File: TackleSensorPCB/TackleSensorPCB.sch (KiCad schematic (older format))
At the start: 26 parts, among them J1 PJ-037A, J2 Conn_01x03_Male, J3 Conn_01x04_Male, J4 Conn_01x07_Male, Q1 2N7002, Q2 2N7002, SW1 SW_DPST_x2, U1 TPS62172DSG, U2 MSP430FR2433IRGER, U3 MMA8452QR1

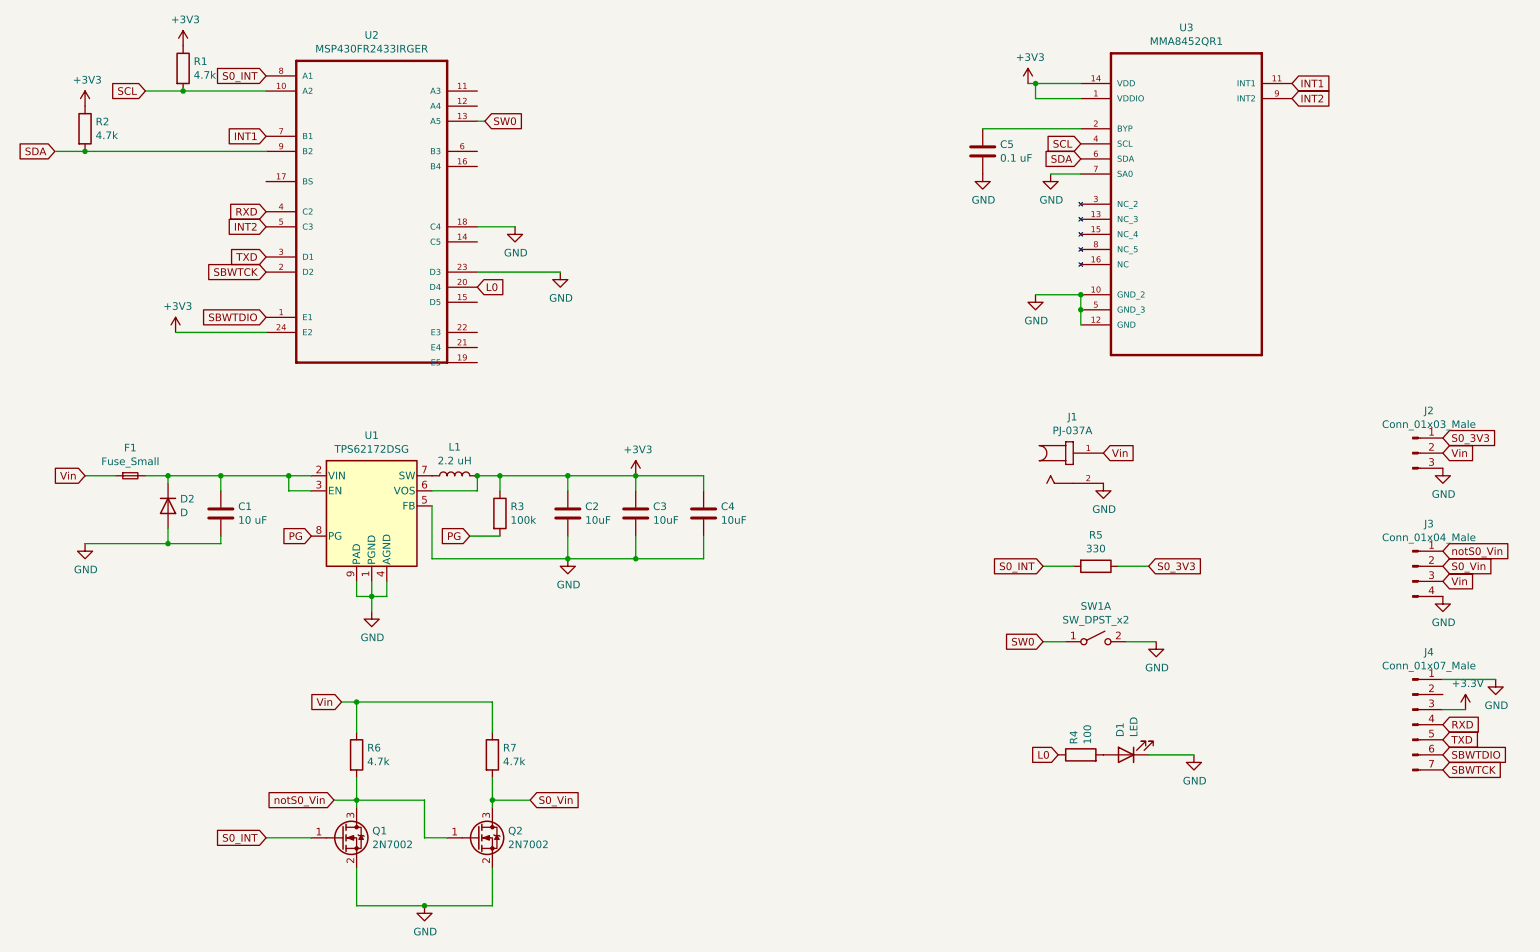
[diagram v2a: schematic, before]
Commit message: Updated to LS2
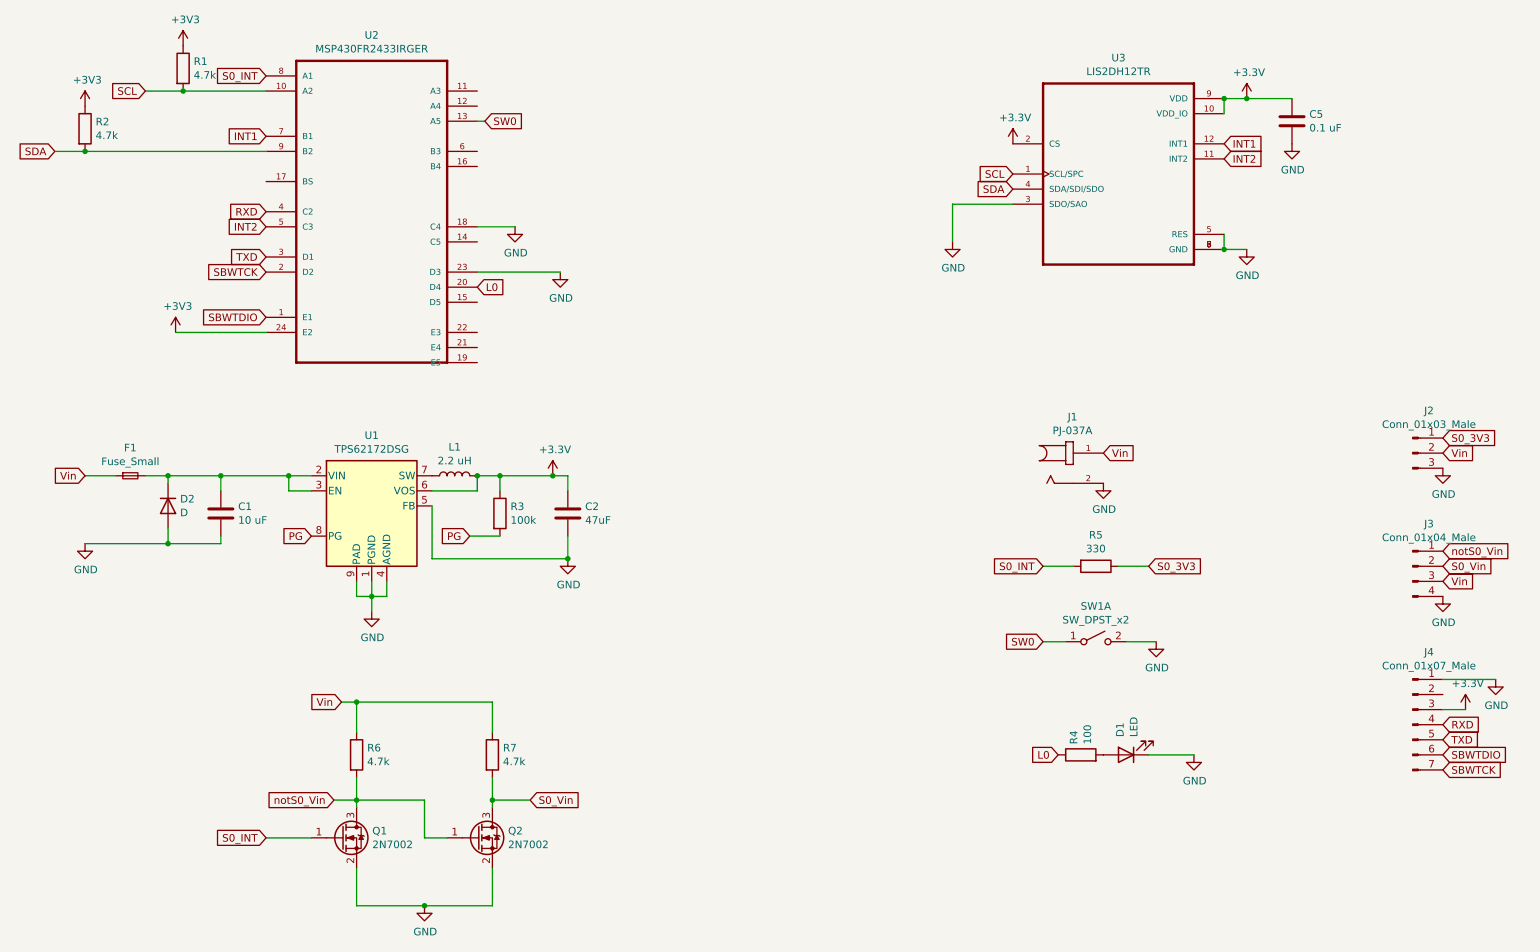
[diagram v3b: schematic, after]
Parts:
- removed C3, C4: 10uF, Capacitor_SMD:C_0402_1005Metric, symbol Device:C
- removed U3: MMA8452QR1, MMA8452QR1:QFN50P300X300X100-16N, symbol MMA8452QR1:MMA8452QR1
- added U3: LIS2DH12TR, LIS2DH12TR:PQFN50P200X200100-12N, symbol LIS2DH12TR:LIS2DH12TR
- C2: value 10uF -> 47uF
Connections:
- net +3V3: now also C5.1, U3.10 (VDD_IO), U3.2 (CS), U3.9 (VDD)
- net GND: now also U3.3 (SDO/SAO), U3.5 (RES), U3.6 (GND), U3.7 (GND), U3.8 (GND)
- net INT1: now also U3.12 (INT1)
- net INT2: now also U3.11 (INT2)
- net SCL: now also U3.1 (SCL/SPC)
- net SDA: now also U3.4 (SDA/SDI/SDO)
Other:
- moved on the sheet: C5
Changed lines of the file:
@@
-$EndComp
-$Comp
-L MMA8452QR1:MMA8452QR1 U3
-U 1 1 5F828B59
-P 8300 2300
-F 0 "U3" H 8300 3370 50  0000 C CNN
-F 1 "MMA8452QR1" H 8300 3279 50  0000 C CNN
-F 2 "MMA8452QR1:QFN50P300X300X100-16N" H 8300 2300 50  0001 L BNN
-F 3 "Freescale" H 8300 2300 50  0001 L BNN
-F 4 "QFN-16" H 8300 2300 50  0001 L BNN "Field4"
-F 5 "MMA8452QR1" H 8300 2300 50  0001 L BNN "Field5"
-F 6 "1908022" H 8300 2300 50  0001 L BNN "Field6"
-F 7 "84R7352" H 8300 2300 50  0001 L BNN "Field7"
-	1    8300 2300
-	1    0    0    -1
 $EndComp
 $Comp
@@
 Wire Wire Line
 	3300 4750 3300 4400
-$Comp
-L power:+3V3 #PWR08
-U 1 1 5F839D50
-P 4650 4200
-F 0 "#PWR08" H 4650 4050 50  0001 C CNN
-F 1 "+3V3" H 4665 4373 50  0000 C CNN
-F 2 "" H 4650 4200 50  0001 C CNN
-F 3 "" H 4650 4200 50  0001 C CNN
-	1    4650 4200
-	1    0    0    -1
-$EndComp
-Text GLabel 9000 1600 2    50   Input ~ 0
+Text GLabel 8550 2000 2    50   Input ~ 0
 INT1
-Text GLabel 9000 1700 2    50   Input ~ 0
+Text GLabel 8550 2100 2    50   Input ~ 0
 INT2
 Wire Wire Line
@@
 	1    0    0    -1
 $EndComp
-Wire Wire Line
-	7250 1600 7300 1600
-$Comp
-L power:+3V3 #PWR010
-U 1 1 5F83E38F
-P 7250 1600
-F 0 "#PWR010" H 7250 1450 50  0001 C CNN
-F 1 "+3V3" H 7265 1773 50  0000 C CNN
-F 2 "" H 7250 1600 50  0001 C CNN
-F 3 "" H 7250 1600 50  0001 C CNN
-	1    7250 1600
-	1    0    0    -1
-$EndComp
-Wire Wire Line
-	7600 1700 7300 1700
-Wire Wire Line
-	7300 1700 7300 1600
-Connection ~ 7300 1600
-Wire Wire Line
-	7300 1600 7600 1600
-Wire Wire Line
-	7600 2200 7400 2200
-$Comp
-L power:GND #PWR012
-U 1 1 5F8405C5
-P 7400 2200
-F 0 "#PWR012" H 7400 1950 50  0001 C CNN
-F 1 "GND" H 7405 2027 50  0000 C CNN
-F 2 "" H 7400 2200 50  0001 C CNN
-F 3 "" H 7400 2200 50  0001 C CNN
-	1    7400 2200
-	1    0    0    -1
-$EndComp
 $Comp
 L Device:C C5
 U 1 1 5F841354
-P 6950 2050
-F 0 "C5" H 7065 2096 50  0000 L CNN
-F 1 "0.1 uF" H 7065 2005 50  0000 L CNN
-F 2 "Capacitor_SMD:C_0402_1005Metric" H 6988 1900 50  0001 C CNN
-F 3 "~" H 6950 2050 50  0001 C CNN
-	1    6950 2050
-	1    0    0    -1
-$EndComp
-Wire Wire Line
-	7600 3100 7600 3000
-Wire Wire Line
-	7600 3000 7300 3000
-Connection ~ 7600 3000
-$Comp
-L power:GND #PWR011
-U 1 1 5F84AED0
-P 7300 3000
-F 0 "#PWR011" H 7300 2750 50  0001 C CNN
-F 1 "GND" H 7305 2827 50  0000 C CNN
-F 2 "" H 7300 3000 50  0001 C CNN
-F 3 "" H 7300 3000 50  0001 C CNN
-	1    7300 3000
-	1    0    0    -1
-$EndComp
-Wire Wire Line
-	7600 3200 7600 3100
-Connection ~ 7600 3100
-Text GLabel 7600 2000 0    50   Input ~ 0
+P 9000 1850
+F 0 "C5" H 9115 1896 50  0000 L CNN
+F 1 "0.1 uF" H 9115 1805 50  0000 L CNN
+F 2 "Capacitor_SMD:C_0402_1005Metric" H 9038 1700 50  0001 C CNN
+F 3 "~" H 9000 1850 50  0001 C CNN
+	1    9000 1850
+	1    0    0    -1
+$EndComp
+Text GLabel 7150 2200 0    50   Input ~ 0
 SCL
-Text GLabel 7600 2100 0    50   Input ~ 0
+Text GLabel 7150 2300 0    50   Input ~ 0
 SDA
-Wire Wire Line
-	6950 1900 7600 1900
 $Comp
 L Device:LED D1
@@
 	0    -1   -1   0
 $EndComp
-Connection ~ 4200 4200
-Wire Wire Line
-	4200 4200 4650 4200
-Wire Wire Line
-	3750 4200 4200 4200
+Wire Wire Line
+	3750 4200 4100 4200
 $Comp
 L Device:C C2
@@
 P 4200 4450
 F 0 "C2" H 4315 4496 50  0000 L CNN
-F 1 "10uF" H 4315 4405 50  0000 L CNN
+F 1 "47uF" H 4315 4405 50  0000 L CNN
 F 2 "Capacitor_SMD:C_0402_1005Metric" H 4238 4300 50  0001 C CNN
 F 3 "~" H 4200 4450 50  0001 C CNN
@@
 Wire Wire Line
 	4200 4200 4200 4300
-$Comp
-L Device:C C3
-U 1 1 5F841E73
-P 4650 4450
-F 0 "C3" H 4765 4496 50  0000 L CNN
-F 1 "10uF" H 4765 4405 50  0000 L CNN
-F 2 "Capacitor_SMD:C_0402_1005Metric" H 4688 4300 50  0001 C CNN
-F 3 "~" H 4650 4450 50  0001 C CNN
-	1    4650 4450
-	1    0    0    -1
-$EndComp
-Wire Wire Line
-	4650 4200 4650 4300
-$Comp
-L Device:C C4
-U 1 1 5F8433F9
-P 5100 4450
-F 0 "C4" H 5215 4496 50  0000 L CNN
-F 1 "10uF" H 5215 4405 50  0000 L CNN
-F 2 "Capacitor_SMD:C_0402_1005Metric" H 5138 4300 50  0001 C CNN
-F 3 "~" H 5100 4450 50  0001 C CNN
-	1    5100 4450
-	1    0    0    -1
-$EndComp
-Wire Wire Line
-	5100 4200 5100 4300
-Wire Wire Line
-	4200 4750 4650 4750
-Wire Wire Line
-	4650 4750 4650 4600
-Wire Wire Line
-	4650 4750 5100 4750
-Wire Wire Line
-	5100 4750 5100 4600
-Connection ~ 4650 4750
-Wire Wire Line
-	4650 4200 5100 4200
-Connection ~ 4650 4200
 $Comp
 L Device:Fuse_Small F1
@@
 L power:GND #PWR0101
 U 1 1 5F86DE04
-P 6950 2200
-F 0 "#PWR0101" H 6950 1950 50  0001 C CNN
-F 1 "GND" H 6955 2027 50  0000 C CNN
-F 2 "" H 6950 2200 50  0001 C CNN
-F 3 "" H 6950 2200 50  0001 C CNN
-	1    6950 2200
+P 9000 2000
+F 0 "#PWR0101" H 9000 1750 50  0001 C CNN
+F 1 "GND" H 9005 1827 50  0000 C CNN
+F 2 "" H 9000 2000 50  0001 C CNN
+F 3 "" H 9000 2000 50  0001 C CNN
+	1    9000 2000
 	1    0    0    -1
 $EndComp
@@
 Connection ~ 1650 1650
 $Comp
-L power:+3.3V #PWR?
+L power:+3.3V #PWR0102
 U 1 1 5F87745C
 P 10150 5750
-F 0 "#PWR?" H 10150 5600 50  0001 C CNN
+F 0 "#PWR0102" H 10150 5600 50  0001 C CNN
 F 1 "+3.3V" H 10165 5923 50  0000 C CNN
 F 2 "" H 10150 5750 50  0001 C CNN
@@
 Wire Wire Line
 	10000 5750 10150 5750
+Wire Wire Line
+	7150 2400 6750 2400
+Wire Wire Line
+	6750 2400 6750 2650
+$Comp
+L power:GND #PWR0104
+U 1 1 5F8E4BA7
+P 6750 2650
+F 0 "#PWR0104" H 6750 2400 50  0001 C CNN
+F 1 "GND" H 6755 2477 50  0000 C CNN
+F 2 "" H 6750 2650 50  0001 C CNN
+F 3 "" H 6750 2650 50  0001 C CNN
+	1    6750 2650
+	1    0    0    -1
+$EndComp
+$Comp
+L power:+3.3V #PWR0106
+U 1 1 5F90A1A8
+P 4100 4200
+F 0 "#PWR0106" H 4100 4050 50  0001 C CNN
+F 1 "+3.3V" H 4115 4373 50  0000 C CNN
+F 2 "" H 4100 4200 50  0001 C CNN
+F 3 "" H 4100 4200 50  0001 C CNN
+	1    4100 4200
+	1    0    0    -1
+$EndComp
+Connection ~ 4100 4200
+Wire Wire Line
+	4100 4200 4200 4200
+$Comp
+L LIS2DH12TR:LIS2DH12TR U3
+U 1 1 5F952488
+P 7850 2200
+F 0 "U3" H 7850 2970 50  0000 C CNN
+F 1 "LIS2DH12TR" H 7850 2879 50  0000 C CNN
+F 2 "LIS2DH12TR:PQFN50P200X200100-12N" H 7850 2200 50  0001 L BNN
+F 3 "Good" H 7850 2200 50  0001 L BNN
+F 4 "LIS2DH12TR" H 7850 2200 50  0001 L BNN "Field4"
+F 5 "0.87 USD" H 7850 2200 50  0001 L BNN "Field5"
+F 6 "STMicroelectronics" H 7850 2200 50  0001 L BNN "Field6"
+F 7 "MEMS digital output motion sensor: ultra low-power high performance 3-axes femto accelerometer" H 7850 2200 50  0001 L BNN "Field7"
+F 8 "LGA-12 STMicroelectronics" H 7850 2200 50  0001 L BNN "Field8"
+	1    7850 2200
+	1    0    0    -1
+$EndComp
+$Comp
+L power:+3.3V #PWR08
+U 1 1 5F956CAD
+P 7150 2000
+F 0 "#PWR08" H 7150 1850 50  0001 C CNN
+F 1 "+3.3V" H 7165 2173 50  0000 C CNN
+F 2 "" H 7150 2000 50  0001 C CNN
+F 3 "" H 7150 2000 50  0001 C CNN
+	1    7150 2000
+	1    0    0    -1
+$EndComp
+$Comp
+L power:+3.3V #PWR010
+U 1 1 5F9576C2
+P 8700 1700
+F 0 "#PWR010" H 8700 1550 50  0001 C CNN
+F 1 "+3.3V" H 8715 1873 50  0000 C CNN
+F 2 "" H 8700 1700 50  0001 C CNN
+F 3 "" H 8700 1700 50  0001 C CNN
+	1    8700 1700
+	1    0    0    -1
+$EndComp
+Wire Wire Line
+	8550 1800 8550 1700
+Wire Wire Line
+	8550 1700 8700 1700
+Connection ~ 8550 1700
+Wire Wire Line
+	8700 2700 8550 2700
+Wire Wire Line
+	8550 2600 8550 2700
+Connection ~ 8550 2700
+$Comp
+L power:GND #PWR011
+U 1 1 5F95F5C9
+P 8700 2700
+F 0 "#PWR011" H 8700 2450 50  0001 C CNN
+F 1 "GND" H 8705 2527 50  0000 C CNN
+F 2 "" H 8700 2700 50  0001 C CNN
+F 3 "" H 8700 2700 50  0001 C CNN
+	1    8700 2700
+	1    0    0    -1
+$EndComp
+Wire Wire Line
+	9000 1700 8700 1700
+Connection ~ 8700 1700
 $EndSCHEMATC

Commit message: Completed 3D model
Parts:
- removed SW1: SW_DPST_x2, TS-1187A-B-A-B:SW_TS-1187A-B-A-B, symbol Switch:SW_DPST_x2
- added SW1: FSM4JSMA, FSM4JSMA:TE_FSM4JSMA, symbol FSM4JSMA:FSM4JSMA
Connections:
- net GND: now also SW1.3, SW1.4
- net SW0: now also SW1.1, SW1.2
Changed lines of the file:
@@
 	-1   0    0    1
-$EndComp
-$Comp
-L Switch:SW_DPST_x2 SW1
-U 1 1 5F85059A
-P 7700 5300
-F 0 "SW1" H 7700 5535 50  0000 C CNN
-F 1 "SW_DPST_x2" H 7700 5444 50  0000 C CNN
-F 2 "TS-1187A-B-A-B:SW_TS-1187A-B-A-B" H 7700 5300 50  0001 C CNN
-F 3 "~" H 7700 5300 50  0001 C CNN
-	1    7700 5300
-	1    0    0    -1
 $EndComp
 Text GLabel 7450 6050 0    50   Input ~ 0
@@
 	1    0    0    -1
 $EndComp
-Wire Wire Line
-	7500 5300 7350 5300
-Text GLabel 7350 5300 0    50   Input ~ 0
+Text GLabel 6900 5300 0    50   Input ~ 0
 SW0
 $Comp
@@
 	9000 1700 8700 1700
 Connection ~ 8700 1700
+$Comp
+L FSM4JSMA:FSM4JSMA SW1
+U 1 1 5F922F9E
+P 7550 5300
+F 0 "SW1" H 7500 5665 50  0000 C CNN
+F 1 "FSM4JSMA" H 7500 5574 50  0000 C CNN
+F 2 "FSM4JSMA:TE_FSM4JSMA" H 7550 5300 50  0001 L BNN
+F 3 "50 mA" H 7550 5300 50  0001 L BNN
+F 4 "4-1437565-1" H 7550 5300 50  0001 L BNN "Field4"
+F 5 "Compliant" H 7550 5300 50  0001 L BNN "Field5"
+F 6 "Single Pole - Single Throw" H 7550 5300 50  0001 L BNN "Field6"
+	1    7550 5300
+	1    0    0    -1
+$EndComp
+Wire Wire Line
+	7900 5300 7900 5200
+Wire Wire Line
+	7900 5200 7850 5200
+Wire Wire Line
+	7900 5300 7900 5400
+Wire Wire Line
+	7900 5400 7850 5400
+Connection ~ 7900 5300
+Wire Wire Line
+	7000 5200 7150 5200
+Wire Wire Line
+	7150 5400 7000 5400
+Wire Wire Line
+	7000 5200 7000 5300
+Wire Wire Line
+	6900 5300 7000 5300
+Connection ~ 7000 5300
+Wire Wire Line
+	7000 5300 7000 5400
 $EndSCHEMATC
